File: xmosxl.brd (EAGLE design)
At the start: 130 x 85 mm, 123 parts, among them IC1 74LVC1T45W6-7, IC2 74LVC1T45W6-7, IC3 74LVC1T45W6-7, IC4 74LVC1T45W6-7, IC5 74LVC1T45W6-7, IC6 74ALVC164245DGG_11, IC7 74ALVC164245DGG_11, IC8 74LVC1T45W6-7, IC9 74LVC1T45W6-7, U1 24 MHz Osc. (F535L-24)

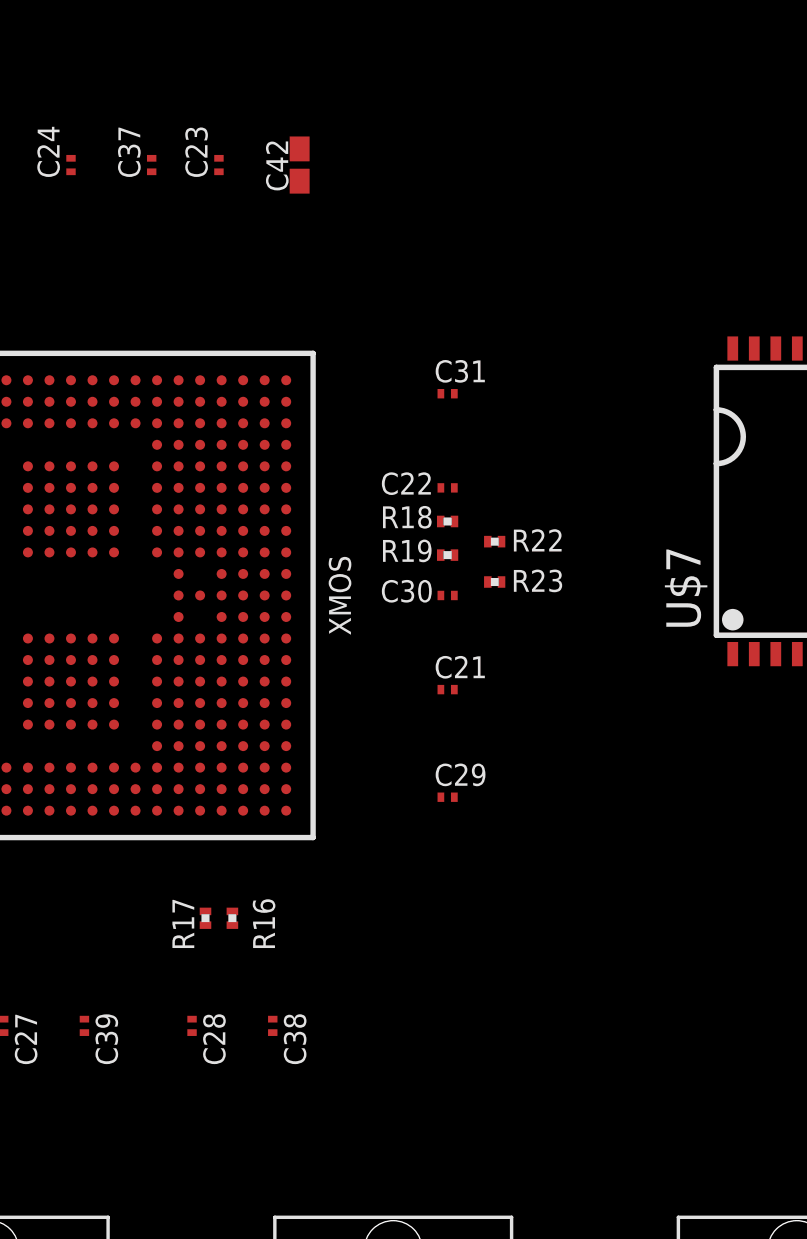
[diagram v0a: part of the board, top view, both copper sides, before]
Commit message: Add the USB RTUNE resistors - per XMOS, no more other connections need to be made to the USB ports.
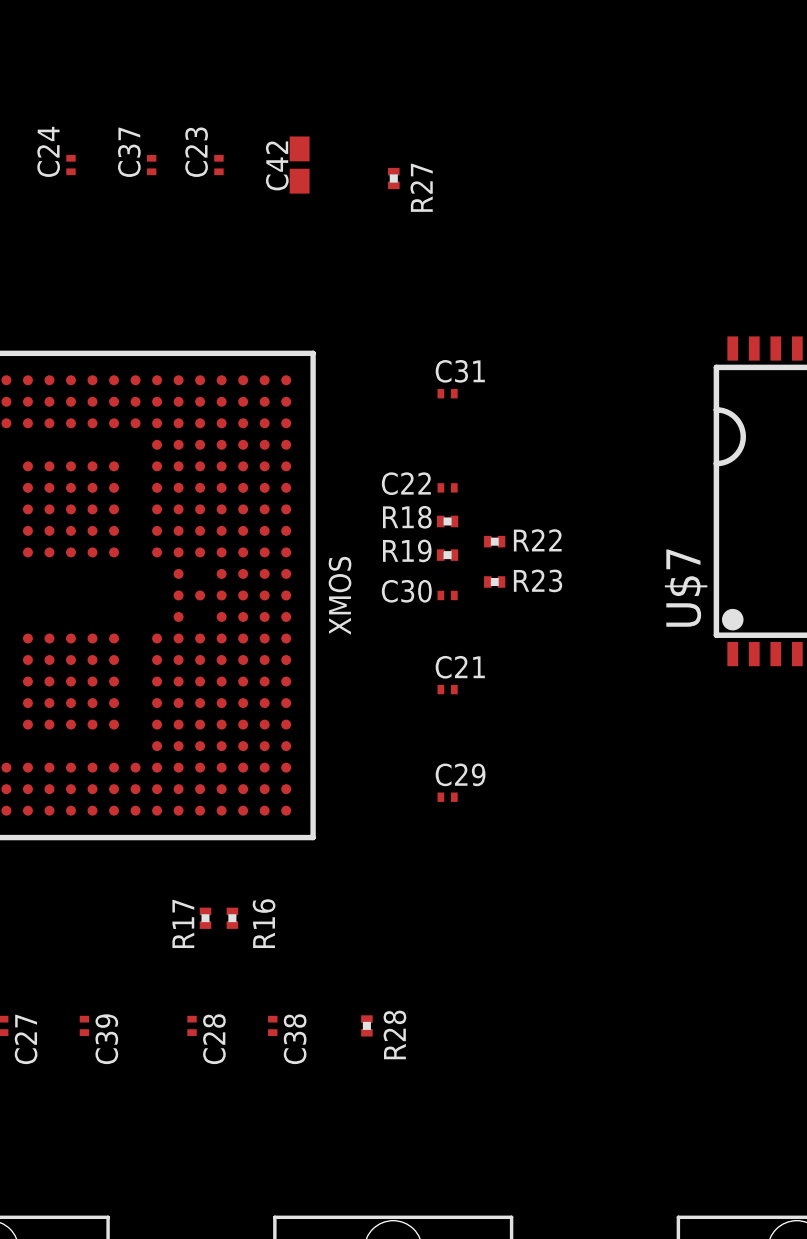
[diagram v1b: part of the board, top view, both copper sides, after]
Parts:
- added R27, R28: 43R2, rcl:R0201
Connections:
- new net N$11: R27.2, XMOS.W16
- new net N$12: R28.2, XMOS.W6
- net GND: now also R27.1, R28.1
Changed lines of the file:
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@@
 <setting verticaltext="up"/>
 </settings>
-<grid distance="5" unitdist="mm" unit="mm" style="lines" multiple="1" display="yes" altdistance="5" altunitdist="mil" altunit="mil"/>
+<grid distance="0.5" unitdist="mm" unit="mm" style="lines" multiple="1" display="yes" altdistance="5" altunitdist="mil" altunit="mil"/>
 <layers>
 <layer number="1" name="Top" color="4" fill="1" visible="yes" active="yes"/>
@@
 <attribute name="VALUE" x="116.5786" y="0.2045" size="1.27" layer="27" rot="R90"/>
 </element>
+<element name="R27" library="rcl" package="R0201" value="43R2" x="80" y="78" smashed="yes" rot="R270">
+<attribute name="NAME" x="80.635" y="78.635" size="0.8128" layer="25" rot="R270"/>
+<attribute name="VALUE" x="78.095" y="78.635" size="1.27" layer="27" rot="R270"/>
+</element>
+<element name="R28" library="rcl" package="R0201" value="43R2" x="79" y="46.5" smashed="yes" rot="R90">
+<attribute name="NAME" x="79.635" y="47.135" size="0.8128" layer="25" rot="R270"/>
+<attribute name="VALUE" x="80.905" y="45.865" size="1.27" layer="27" rot="R90"/>
+</element>
 </elements>
 <signals>
@@
 <contactref element="XMOS" pad="F21"/>
 <contactref element="XMOS" pad="G19"/>
+<contactref element="R28" pad="1"/>
+<contactref element="R27" pad="1"/>
 <wire x1="125.69" y1="61.31" x2="125.69" y2="66.39" width="0" layer="19" extent="1-1"/>
 <wire x1="125.69" y1="56.23" x2="125.69" y2="61.31" width="0" layer="19" extent="1-1"/>
@@
 <wire x1="94.2" y1="71.68" x2="99" y2="71.68" width="0" layer="19" extent="1-1"/>
 <wire x1="92.6" y1="71.68" x2="94.2" y2="71.68" width="0" layer="19" extent="1-1"/>
-<wire x1="113.4" y1="71.68" x2="103" y2="71.68" width="0" layer="19" extent="1-1"/>
-<wire x1="82.25" y1="70" x2="92.6" y2="71.68" width="0" layer="19" extent="1-1"/>
+<wire x1="80" y1="78.255" x2="92.6" y2="71.68" width="0" layer="19" extent="1-1"/>
+<wire x1="82.25" y1="70" x2="80" y2="78.255" width="0" layer="19" extent="1-1"/>
 <wire x1="82.25" y1="66.5" x2="82.25" y2="70" width="0" layer="19" extent="1-1"/>
 <wire x1="83.495" y1="64.5" x2="82.25" y2="66.5" width="0" layer="19" extent="1-1"/>
@@
 <wire x1="82.25" y1="59" x2="82.25" y2="62.5" width="0" layer="19" extent="1-1"/>
 <wire x1="82.25" y1="55" x2="82.25" y2="59" width="0" layer="19" extent="1-1"/>
+<wire x1="79" y1="46.245" x2="82.25" y2="55" width="0" layer="19" extent="1-1"/>
 <wire x1="76" y1="70.5" x2="82.25" y2="70" width="0" layer="19" extent="1-1"/>
 <wire x1="74.4" y1="67.3" x2="76" y2="70.5" width="0" layer="19" extent="1-1"/>
@@
 <wire x1="48.75" y1="83.255" x2="51.5" y2="83.255" width="0" layer="19" extent="1-1"/>
 <wire x1="46" y1="83.255" x2="48.75" y2="83.255" width="0" layer="19" extent="1-1"/>
+<wire x1="113.4" y1="71.68" x2="103" y2="71.68" width="0" layer="19" extent="1-1"/>
 <wire x1="42.75" y1="43.5" x2="53.25" y2="54.5" width="0" layer="19" extent="1-1"/>
 <wire x1="42.25" y1="38.5" x2="42.75" y2="43.5" width="0" layer="19" extent="1-1"/>
@@
 <wire x1="66.4" y1="56.1" x2="65.6" y2="56.1" width="0" layer="19" extent="1-1"/>
 <wire x1="61.6" y1="56.1" x2="63.2" y2="56.9" width="0" layer="19" extent="1-1"/>
-<wire x1="53.75" y1="70.5" x2="61.6" y2="68.9" width="0" layer="19" extent="1-1"/>
-<wire x1="53.755" y1="67.5" x2="53.75" y2="70.5" width="0" layer="19" extent="1-1"/>
+<wire x1="53.755" y1="67.5" x2="61.6" y2="68.9" width="0" layer="19" extent="1-1"/>
+<wire x1="53.75" y1="70.5" x2="53.755" y2="67.5" width="0" layer="19" extent="1-1"/>
 <wire x1="53.75" y1="62.5" x2="53.755" y2="67.5" width="0" layer="19" extent="1-1"/>
 <wire x1="53.75" y1="54.5" x2="61.6" y2="56.1" width="0" layer="19" extent="1-1"/>
@@
 <contactref element="XMOS" pad="Y8"/>
 </signal>
+<signal name="N$11">
+<contactref element="XMOS" pad="W16"/>
+<contactref element="R27" pad="2"/>
+<wire x1="74.4" y1="66.5" x2="80" y2="77.745" width="0" layer="19" extent="1-1"/>
+</signal>
+<signal name="N$12">
+<contactref element="XMOS" pad="W6"/>
+<contactref element="R28" pad="2"/>
+<wire x1="79" y1="46.755" x2="74.4" y2="58.5" width="0" layer="19" extent="1-1"/>
+</signal>
 </signals>
